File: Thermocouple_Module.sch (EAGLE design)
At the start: 1 part, among them U1 INA213

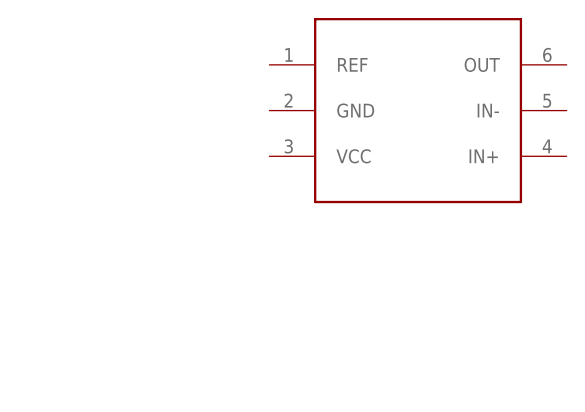
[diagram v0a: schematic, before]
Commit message: added resistor
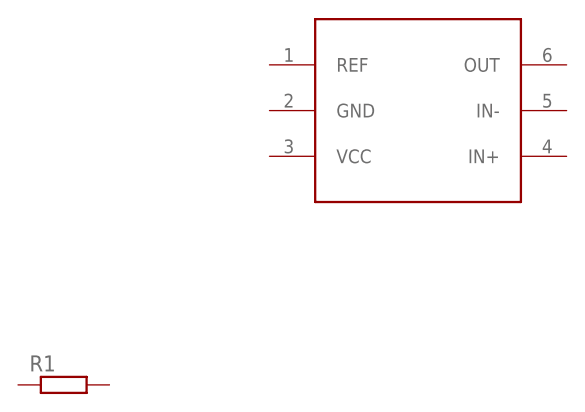
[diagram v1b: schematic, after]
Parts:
- added R1: (no value), rcl:R-EU_0204/7
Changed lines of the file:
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@@
 <drawing>
 <settings>
-<setting alwaysvectorfont="no"/>
+<setting alwaysvectorfont="yes"/>
 <setting verticaltext="up"/>
 </settings>
@@
 <part name="FRAME1" library="frames" library_urn="urn:adsk.eagle:library:229" deviceset="A4L-LOC" device=""/>
 <part name="U1" library="texas" library_urn="urn:adsk.eagle:library:14701157" deviceset="INA213" device="" package3d_urn="urn:adsk.eagle:package:14710703/2"/>
+<part name="R1" library="rcl" library_urn="urn:adsk.eagle:library:13439567" deviceset="R-EU_" device="0204/7" package3d_urn="urn:adsk.eagle:package:14161861/1"/>
 </parts>
 <sheets>
@@
 </instance>
 <instance part="U1" gate="G$1" x="119.38" y="106.68" smashed="yes"/>
+<instance part="R1" gate="G$1" x="78.74" y="76.2" smashed="yes">
+<attribute name="NAME" x="74.93" y="77.6986" size="1.778" layer="95"/>
+<attribute name="VALUE" x="74.93" y="72.898" size="1.778" layer="96"/>
+</instance>
 </instances>
 <busses>
@@
 packages will not be understood (or retained) with this version.
 </note>
+<note version="8.4" severity="warning">
+Since Version 8.4, EAGLE supports properties for SPICE simulation.
+Probes in schematics and SPICE mapping objects found in parts and library devices
+will not be understood with this version. Update EAGLE to the latest version
+for full support of SPICE simulation.
+</note>
 </compatibility>
